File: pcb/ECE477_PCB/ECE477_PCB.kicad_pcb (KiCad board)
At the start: 2 copper layers, 65 x 30 mm, 99 parts, among them J1 DEBUG, J10 ToF 5, J11 Pi Zero, J2 USB_B_Micro, J3 ESC, J4 ELRS, J5 AUX_PWR, J6 ToF 1, J7 ToF 2, J8 ToF 3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

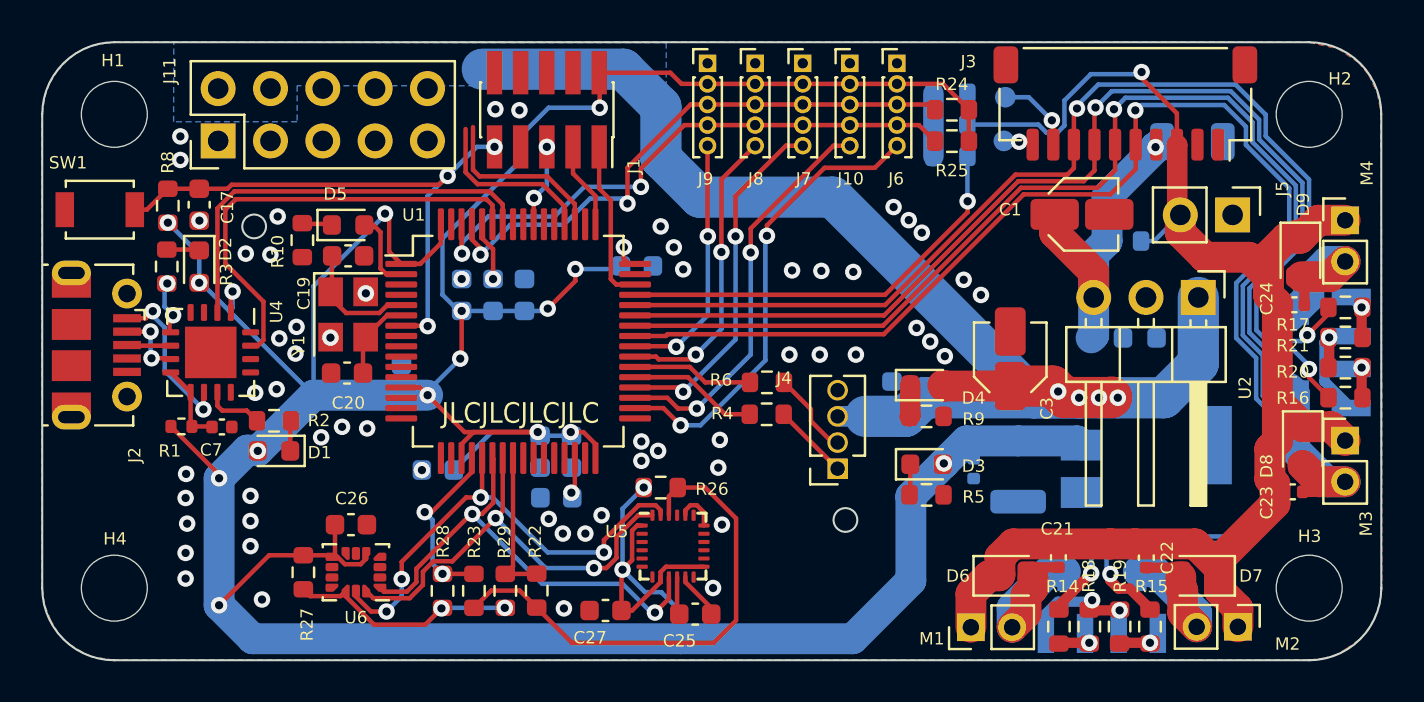
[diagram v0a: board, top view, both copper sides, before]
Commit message: fixed pi zero connector position
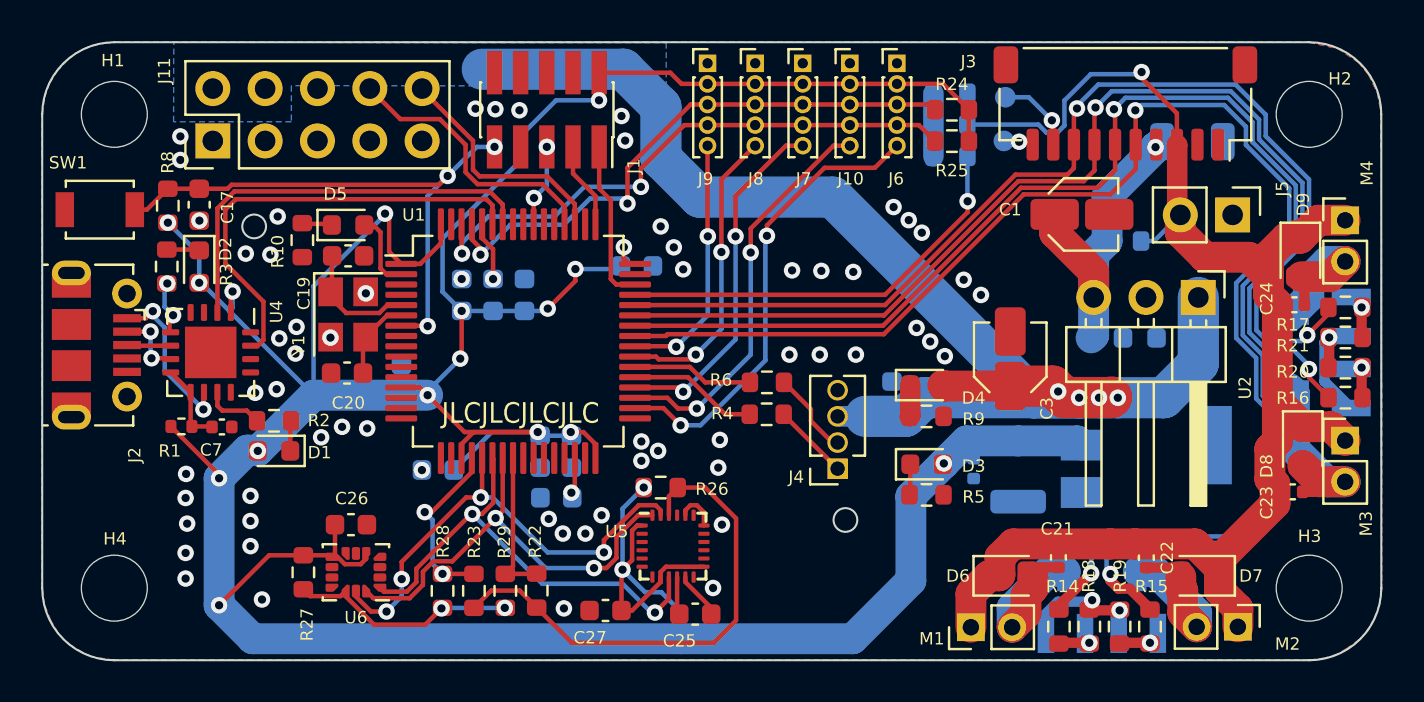
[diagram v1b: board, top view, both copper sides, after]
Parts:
- moved J11 0.26 mm to (56.2, 32.8)
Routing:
- net UART4_RX: track 8.46 -> 13.5 mm
- net UART4_TX: track 8.68 -> 11.6 mm
- net GND: vias 62 -> 65

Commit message: fixed ESC connector placement
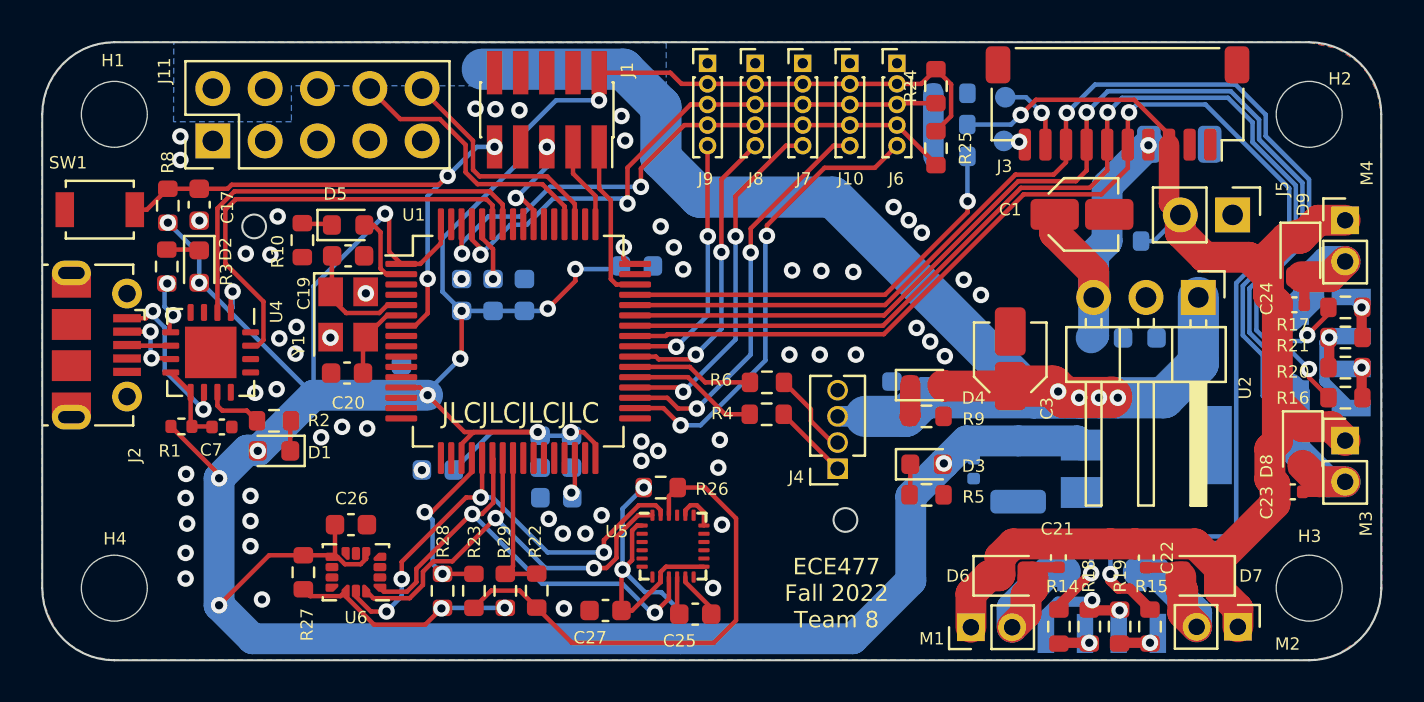
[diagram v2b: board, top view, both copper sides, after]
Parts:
- moved R24 1.38 mm to (91.3, 30.1), turned to -90 degrees
- moved R25 0.85 mm to (91.3, 33.1), turned to -90 degrees
- moved C29 0.65 mm to (103.1, 32.9)
- moved J3 0.38 mm to (100.1, 30.9)
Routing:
- net +BATT: track 76.0 -> 72.5 mm
- net MOTOR_A: track 69.8 -> 68.0 mm
- net SYS_JTCL-SWO: track 4.02 -> 4.90 mm
- net Net-(J3-Pad10): track 1.47 -> 0.76 mm
- net MOTOR_D: track 54.3 -> 53.6 mm
- net I2C1_SDA: track 28.1 -> 28.7 mm
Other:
- board text added: "ECE477 Fall 2022 Team 8"
- board text added: "Flight Controller Rev. 0.0 Michael Langford Santiago Delgado Jonathan Wosiak Owen Mandel"

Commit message: fixed vias, added test points, fixed ground plane in some spots
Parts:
- added TP3: TX, TestPoint:TestPoint_Pad_D1.0mm, F.Cu at (65.3, 49.9)
- added TP4: TX, TestPoint:TestPoint_Pad_D1.0mm, F.Cu at (63.1, 48.2)
- added TP5: TX, TestPoint:TestPoint_Pad_D1.0mm, F.Cu at (80.5, 47.1)
- C18: moved to F.Cu
- turned D2 to 90 degrees
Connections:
- U1 pad 33: unconnected-(U1-Pad33) -> Net-(U1-Pad33)
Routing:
- net Net-(U1-Pad33): track 0.00 -> 4.18 mm
- net USART2_RX: track 0.00 -> 3.50 mm
- net SYS_JTCL-SWO: track 4.90 -> 8.27 mm
- net USART2_TX: track 0.00 -> 3.35 mm
- net +10V: track 15.4 -> 17.7 mm, vias 1 -> 2
- net Net-(J3-Pad10): track 0.76 -> 2.98 mm
- net Net-(R22-Pad2): track 24.5 -> 26.5 mm
- net Net-(R27-Pad1): track 11.2 -> 13.0 mm
- net +3V3: track 204.9 -> 205.8 mm, vias 19 -> 18
- net I2C1_SDA: track 28.7 -> 27.8 mm
- net Net-(D2-Pad1): track 1.59 -> 2.26 mm
- net USART1_RX: track 22.1 -> 21.4 mm
- net SPI1_MOSI: track 21.7 -> 22.3 mm
- net SPI1_MISO: track 22.8 -> 23.3 mm
- net Net-(C18-Pad1): track 1.75 -> 1.98 mm, vias 1 -> 0
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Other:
- outline, holes or cut-outs redrawn
- board text removed: "JLCJLCJLCJLC"

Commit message: fixed more ground plane risks
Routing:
- net Net-(R22-Pad2): track 26.5 -> 25.4 mm
- net +3V3: track 205.8 -> 206.5 mm, vias 18 -> 19
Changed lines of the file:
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@@
   (segment (start 74.7522 48.1452) (end 74.7522 46.8122) (width 0.22) (layer "F.Cu") (net 23))
   (segment (start 91.2876 32.2834) (end 92.0242 31.5468) (width 0.22) (layer "F.Cu") (net 23))
+  (segment (start 77.006 29.4454) (end 77.8002 28.6512) (width 0.22) (layer "F.Cu") (net 23))
   (segment (start 55.5938 38.0678) (end 56.515 38.989) (width 0.22) (layer "F.Cu") (net 23))
   (segment (start 90.5736 29.988) (end 89.3958 29.988) (width 0.22) (layer "F.Cu") (net 23))
@@
   (segment (start 91.6305 48.4505) (end 92.7626 47.3184) (width 1) (layer "F.Cu") (net 23))
   (segment (start 62.1154 51.3842) (end 62.1154 52.7978) (width 0.22) (layer "F.Cu") (net 23))
-  (segment (start 78.9344 29.9854) (end 80.1984 29.9854) (width 0.22) (layer "F.Cu") (net 23))
   (segment (start 76.0228 55.5498) (end 76.0228 53.6188) (width 0.22) (layer "F.Cu") (net 23))
   (segment (start 76.0228 53.6188) (end 76.073 53.5686) (width 0.22) (layer "F.Cu") (net 23))
-  (segment (start 78.3944 29.4454) (end 78.9344 29.9854) (width 0.22) (layer "F.Cu") (net 23))
   (segment (start 66.2406 44.7256) (end 66.6134 45.0984) (width 0.22) (layer "F.Cu") (net 23))
   (segment (start 54.0024 36.7274) (end 54.0044 36.7254) (width 0.22) (layer "F.Cu") (net 23))
@@
   (segment (start 57.0582 41.0835) (end 57.0582 40.195129) (width 0.22) (layer "F.Cu") (net 23))
   (segment (start 92.0242 31.5468) (end 92.0242 30.0106) (width 0.22) (layer "F.Cu") (net 23))
-  (segment (start 74.9394 29.4454) (end 78.3944 29.4454) (width 0.22) (layer "F.Cu") (net 23))
   (segment (start 62.595016 53.3037) (end 63.360406 53.3037) (width 0.22) (layer "F.Cu") (net 23))
   (segment (start 77.0238 51.4256) (end 76.781104 51.4256) (width 0.22) (layer "F.Cu") (net 23))
@@
   (segment (start 78.181104 53.4256) (end 80.0238 53.4256) (width 0.22) (layer "F.Cu") (net 23))
   (segment (start 66.6134 45.0984) (end 68.3272 46.8122) (width 0.22) (layer "F.Cu") (net 23))
+  (segment (start 74.9394 29.4454) (end 77.006 29.4454) (width 0.22) (layer "F.Cu") (net 23))
   (segment (start 77.9238 54.168296) (end 77.9238 53.9256) (width 0.22) (layer "F.Cu") (net 23))
   (segment (start 54.184 36.7274) (end 55.5244 38.0678) (width 0.22) (layer "F.Cu") (net 23))
@@
   (via (at 54.356 47.7012) (size 0.8) (drill 0.4) (layers "F.Cu" "B.Cu") (net 23))
   (via (at 69.0626 40.3352) (size 0.8) (drill 0.4) (layers "F.Cu" "B.Cu") (net 23))
+  (via (at 77.8002 28.6512) (size 0.8) (drill 0.4) (layers "F.Cu" "B.Cu") (net 23))
   (via (at 66.6134 45.0984) (size 0.8) (drill 0.4) (layers "F.Cu" "B.Cu") (net 23))
   (via (at 76.01408 50.42627) (size 0.8) (drill 0.4) (layers "F.Cu" "B.Cu") (net 23))
@@
   (via (at 76.1238 37.5666) (size 0.8) (drill 0.4) (layers "F.Cu" "B.Cu") (net 23))
   (segment (start 64.5444 36.3354) (end 61.0736 39.8062) (width 0.22) (layer "B.Cu") (net 23))
+  (segment (start 77.8002 28.6512) (end 79.137 29.988) (width 0.22) (layer "B.Cu") (net 23))
   (segment (start 71.3124 41.0096) (end 72.3302 41.0096) (width 0.22) (layer "B.Cu") (net 23))
   (segment (start 71.8313 31.192736) (end 72.239136 30.7849) (width 0.22) (layer "B.Cu") (net 23))
   (segment (start 71.3124 41.0096) (end 69.7884 41.0096) (width 0.22) (layer "B.Cu") (net 23))
+  (segment (start 79.137 29.988) (end 80.201 29.988) (width 0.22) (layer "B.Cu") (net 23))
   (segment (start 66.6134 44.9064) (end 68.1944 43.3254) (width 0.22) (layer "B.Cu") (net 23))
   (segment (start 74.3205 30.7849) (end 74.4474 30.9118) (width 0.22) (layer "B.Cu") (net 23))
@@
   (segment (start 70.7576 53.3986) (end 70.3834 53.7728) (width 0.22) (layer "F.Cu") (net 100))
   (segment (start 70.3834 53.7728) (end 71.8942 53.7728) (width 0.22) (layer "F.Cu") (net 100))
-  (segment (start 68.8594 55.7022) (end 70.2818 57.1246) (width 0.22) (layer "F.Cu") (net 101))
-  (segment (start 73.6224 57.1246) (end 73.7108 57.1246) (width 0.22) (layer "F.Cu") (net 101))
+  (segment (start 72.581 56.0832) (end 71.9074 55.4096) (width 0.22) (layer "F.Cu") (net 101))
+  (segment (start 72.9874 56.4896) (end 81.1276 56.4896) (width 0.22) (layer "F.Cu") (net 101))
   (segment (start 78.7522 49.5808) (end 78.3238 50.0092) (width 0.22) (layer "F.Cu") (net 101))
+  (segment (start 81.1276 56.4896) (end 81.5848 56.0324) (width 0.22) (layer "F.Cu") (net 101))
+  (segment (start 81.5848 56.0324) (end 81.5848 51.0794) (width 0.22) (layer "F.Cu") (net 101))
   (segment (start 78.3238 50.0092) (end 78.3238 50.9256) (width 0.22) (layer "F.Cu") (net 101))
-  (segment (start 80.4926 57.1246) (end 81.5848 56.0324) (width 0.22) (layer "F.Cu") (net 101))
+  (segment (start 68.8594 55.7022) (end 69.2404 56.0832) (width 0.22) (layer "F.Cu") (net 101))
+  (segment (start 69.2404 56.0832) (end 72.581 56.0832) (width 0.22) (layer "F.Cu") (net 101))
   (segment (start 80.0862 49.5808) (end 78.7522 49.5808) (width 0.22) (layer "F.Cu") (net 101))
+  (segment (start 68.8594 55.4218) (end 68.8594 55.7022) (width 0.22) (layer "F.Cu") (net 101))
   (segment (start 81.5848 51.0794) (end 80.0862 49.5808) (width 0.22) (layer "F.Cu") (net 101))
-  (segment (start 68.8594 55.4218) (end 68.8594 55.7022) (width 0.22) (layer "F.Cu") (net 101))
-  (segment (start 71.9074 55.4096) (end 73.6224 57.1246) (width 0.22) (layer "F.Cu") (net 101))
-  (segment (start 70.2818 57.1246) (end 73.7108 57.1246) (width 0.22) (layer "F.Cu") (net 101))
-  (segment (start 73.7108 57.1246) (end 80.4926 57.1246) (width 0.22) (layer "F.Cu") (net 101))
-  (segment (start 81.5848 56.0324) (end 81.5848 51.0794) (width 0.22) (layer "F.Cu") (net 101))
+  (segment (start 71.9074 55.4096) (end 72.9874 56.4896) (width 0.22) (layer "F.Cu") (net 101))
   (segment (start 66.811651 50.7746) (end 66.4718 50.7746) (width 0.22) (layer "F.Cu") (net 102))
   (segment (start 68.7576 48.828651) (end 66.811651 50.7746) (width 0.22) (layer "F.Cu") (net 102))

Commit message: fixed more ground plane risks
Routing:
- net +3V3: track 206.5 -> 206.9 mm, vias 19 -> 18
- net GND: vias 72 -> 73
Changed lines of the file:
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@@
   (segment (start 74.7576 48.1506) (end 74.7522 48.1452) (width 0.22) (layer "F.Cu") (net 23))
   (segment (start 91.2876 29.274) (end 90.5736 29.988) (width 0.22) (layer "F.Cu") (net 23))
+  (segment (start 66.9918 45.0984) (end 66.6134 45.0984) (width 0.22) (layer "F.Cu") (net 23))
   (segment (start 80.201 29.988) (end 82.5124 29.988) (width 0.22) (layer "F.Cu") (net 23))
   (segment (start 76.0228 55.5498) (end 76.542296 55.5498) (width 0.22) (layer "F.Cu") (net 23))
@@
   (segment (start 64.5444 36.2854) (end 64.7444 36.4854) (width 0.22) (layer "F.Cu") (net 23))
   (segment (start 68.3272 46.8122) (end 68.9102 46.8122) (width 0.22) (layer "F.Cu") (net 23))
-  (segment (start 69.0626 42.4572) (end 69.0626 40.3352) (width 0.22) (layer "F.Cu") (net 23))
   (segment (start 63.360406 53.3037) (end 63.632 53.032106) (width 0.22) (layer "F.Cu") (net 23))
   (segment (start 74.7522 48.1452) (end 74.7522 46.8122) (width 0.22) (layer "F.Cu") (net 23))
   (segment (start 91.2876 32.2834) (end 92.0242 31.5468) (width 0.22) (layer "F.Cu") (net 23))
   (segment (start 77.006 29.4454) (end 77.8002 28.6512) (width 0.22) (layer "F.Cu") (net 23))
+  (segment (start 69.0626 40.3352) (end 69.0626 43.0276) (width 0.22) (layer "F.Cu") (net 23))
   (segment (start 55.5938 38.0678) (end 56.515 38.989) (width 0.22) (layer "F.Cu") (net 23))
   (segment (start 90.5736 29.988) (end 89.3958 29.988) (width 0.22) (layer "F.Cu") (net 23))
@@
   (segment (start 54.0004 36.7274) (end 54.0024 36.7274) (width 0.22) (layer "F.Cu") (net 23))
   (segment (start 64.7444 38.1374) (end 65.3326 38.7256) (width 0.22) (layer "F.Cu") (net 23))
-  (segment (start 68.1944 43.3254) (end 69.0626 42.4572) (width 0.22) (layer "F.Cu") (net 23))
   (segment (start 62.235015 52.9437) (end 62.595016 53.3037) (width 0.22) (layer "F.Cu") (net 23))
   (segment (start 57.0582 40.195129) (end 57.164838 40.088491) (width 0.22) (layer "F.Cu") (net 23))
@@
   (segment (start 77.9238 54.1692) (end 77.9238 53.9256) (width 0.22) (layer "F.Cu") (net 23))
   (segment (start 58.3692 47.8028) (end 57.817 47.8028) (width 0.22) (layer "F.Cu") (net 23))
+  (segment (start 69.0626 43.0276) (end 66.9918 45.0984) (width 0.22) (layer "F.Cu") (net 23))
   (segment (start 65.3326 44.7256) (end 66.2406 44.7256) (width 0.22) (layer "F.Cu") (net 23))
   (segment (start 80.1984 29.9854) (end 80.201 29.988) (width 0.22) (layer "F.Cu") (net 23))
@@
   (via (at 57.164838 40.088491) (size 0.8) (drill 0.4) (layers "F.Cu" "B.Cu") (net 23))
   (via (at 72.4444 40.8954) (size 0.8) (drill 0.4) (layers "F.Cu" "B.Cu") (net 23))
-  (via (at 68.1944 43.3254) (size 0.8) (drill 0.4) (layers "F.Cu" "B.Cu") (net 23))
   (via (at 56.4896 55.2958) (size 0.8) (drill 0.4) (layers "F.Cu" "B.Cu") (net 23))
   (via (at 76.073 53.5686) (size 0.8) (drill 0.4) (layers "F.Cu" "B.Cu") (net 23))
@@
   (segment (start 71.3124 41.0096) (end 69.7884 41.0096) (width 0.22) (layer "B.Cu") (net 23))
   (segment (start 79.137 29.988) (end 80.201 29.988) (width 0.22) (layer "B.Cu") (net 23))
-  (segment (start 66.6134 44.9064) (end 68.1944 43.3254) (width 0.22) (layer "B.Cu") (net 23))
   (segment (start 74.3205 30.7849) (end 74.4474 30.9118) (width 0.22) (layer "B.Cu") (net 23))
   (segment (start 57.164838 39.511838) (end 57.164838 40.088491) (width 0.22) (layer "B.Cu") (net 23))
@@
   (segment (start 78.8924 56.9214) (end 58.1152 56.9214) (width 1.5) (layer "B.Cu") (net 23))
   (segment (start 72.3302 41.0096) (end 72.4444 40.8954) (width 0.22) (layer "B.Cu") (net 23))
-  (segment (start 66.6134 45.0984) (end 66.6134 44.9064) (width 0.22) (layer "B.Cu") (net 23))
   (segment (start 77.9526 54.6608) (end 78.6892 55.3974) (width 0.22) (layer "B.Cu") (net 23))
   (segment (start 61.0736 45.0984) (end 66.6134 45.0984) (width 1.5) (layer "B.Cu") (net 23))
   (segment (start 65.3434 45.1876) (end 65.4326 45.0984) (width 0.22) (layer "B.Cu") (net 23))
   (segment (start 71.82 46.8122) (end 72.0744 47.0666) (width 0.22) (layer "B.Cu") (net 23))
+  (segment (start 66.6134 45.0984) (end 66.6134 44.918) (width 0.22) (layer "B.Cu") (net 23))
   (segment (start 75.9984 38.8246) (end 76.1238 38.6992) (width 0.22) (layer "B.Cu") (net 23))
   (segment (start 67.8834 47.839) (end 68.9102 46.8122) (width 0.22) (layer "B.Cu") (net 23))
@@
   (via (at 92.6338 39.497) (size 0.8) (drill 0.4) (layers "F.Cu" "B.Cu") (free) (net 24))
   (via (at 110.3757 42.2976) (size 0.8) (drill 0.4) (layers "F.Cu" "B.Cu") (net 24))
+  (via (at 67.7672 42.9006) (size 0.8) (drill 0.4) (layers "F.Cu" "B.Cu") (free) (net 24))
   (via (at 54.61 33.6804) (size 0.8) (drill 0.4) (layers "F.Cu" "B.Cu") (free) (net 24))
   (via (at 54.864 50.0888) (size 0.8) (drill 0.4) (layers "F.Cu" "B.Cu") (free) (net 24))

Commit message: fixed potential issues with mounting holes
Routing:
- net MOTOR_A: track 68.0 -> 68.9 mm
- net MOTOR_B: track 70.4 -> 69.6 mm
